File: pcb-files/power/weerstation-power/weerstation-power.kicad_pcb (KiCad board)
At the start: 2 copper layers, 100 x 100 mm, 37 parts, among them J1 analoog bord connector power, J10 5v_power, J11 3.3v_power, J12 servo_power, J2 digitaal bord connector power, J3 zonnepanelen_12.3v, J4 batterij_laden_12.3v, J5 batterij_load_12.3v, J6 batterij_12.3v, J7 power_monitor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

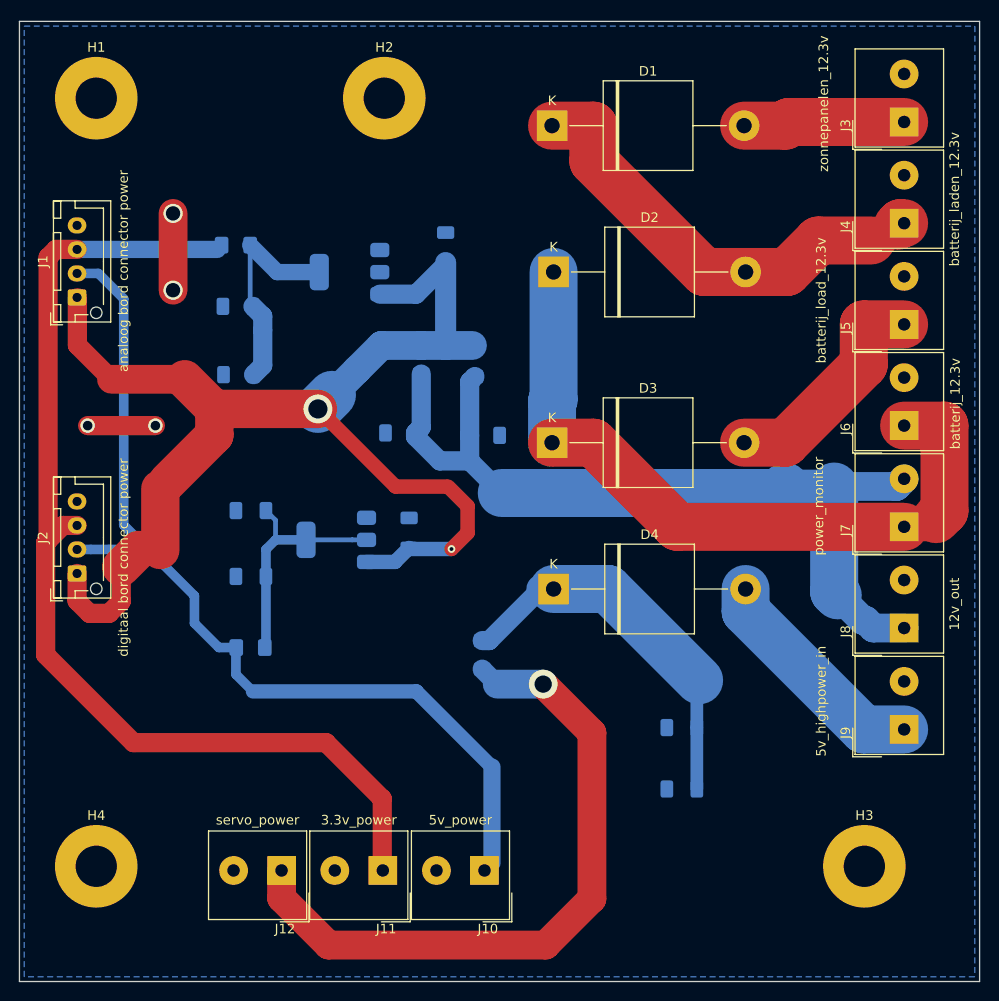
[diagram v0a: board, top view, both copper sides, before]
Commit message: update pcb files better layout and grounding inproved
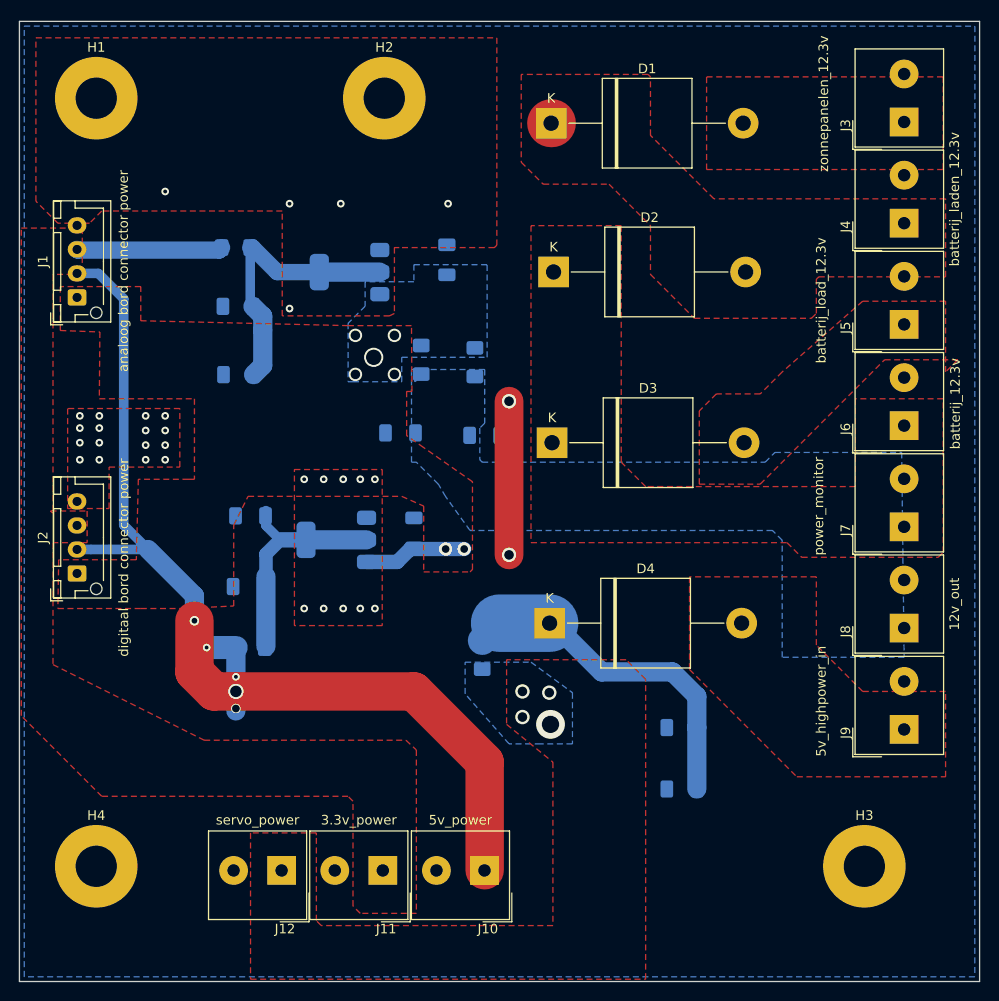
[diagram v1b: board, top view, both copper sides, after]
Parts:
- moved C5 7.92 mm to (35.8, 70.9)
- moved C6 6.31 mm to (36.1, 63.5)
- moved D4 3.58 mm to (67.2, 74.7)
- moved C1 1.28 mm to (56.5, 36.8)
- moved C4 0.51 mm to (53.1, 65.3)
- moved D1 0.27 mm to (67.4, 22.6)
- moved F4 0.25 mm to (34.5, 35.6)
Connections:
- net Net-(D1-A) renamed +VDC
- net Net-(D1-K) renamed +BATT
- net Net-(D2-K) renamed VDD
- net Net-(D3-A) renamed VDC
- net Net-(D4-A) renamed +5VP
- net Net-(J7-Pin_2) renamed VBUS
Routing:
- net +12L: track 137.7 -> 11.6 mm, vias 2 -> 7
- net +3.3V: track 115.5 -> 15.7 mm
- net VBUS: track 89.7 -> 0.20 mm
- net VDD: track 76.5 -> 0.23 mm
- net +5VL: track 70.7 -> 0.00 mm, vias 1 -> 4
- net +BATT: track 47.2 -> 0.08 mm
- net VDC: track 24.2 -> 0.00 mm
- net +5VP: track 23.9 -> 0.00 mm
- net +VDC: track 16.8 -> 0.00 mm
- net +5V: track 100.2 -> 115.1 mm, vias 0 -> 5
- net Net-(U1-VO): track 22.8 -> 28.7 mm
- net Net-(D4-K): track 40.2 -> 35.9 mm
- net GND: track 15.1 -> 16.0 mm, vias 4 -> 33
- added copper zone on B.Cu, net +12L
- added copper zone on F.Cu, net +12L
- added copper zone on F.Cu, net +3.3V
- added copper zone on B.Cu, net +5VL
- added copper zone on F.Cu, net +5VL
- added copper zone on F.Cu, net +5VP
- added copper zone on F.Cu, net +BATT
- added copper zone on F.Cu, net +VDC
- added copper zone on F.Cu, net GND
- added copper zone on B.Cu, net VBUS
- added copper zone on F.Cu, net VDC
- added copper zone on F.Cu, net VDD
